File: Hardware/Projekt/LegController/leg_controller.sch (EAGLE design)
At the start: 53 parts, among them IC1 TS1117-3.3, IC3 ATXMEGA32A4U-AU, J1 22-27-2031-03, J2 22-27-2031-03, Q1 16MHz/18pF, T1 BC847SMD, T3 BC847SMD, T4 BC847SMD, U1 INA3221AIRGVT

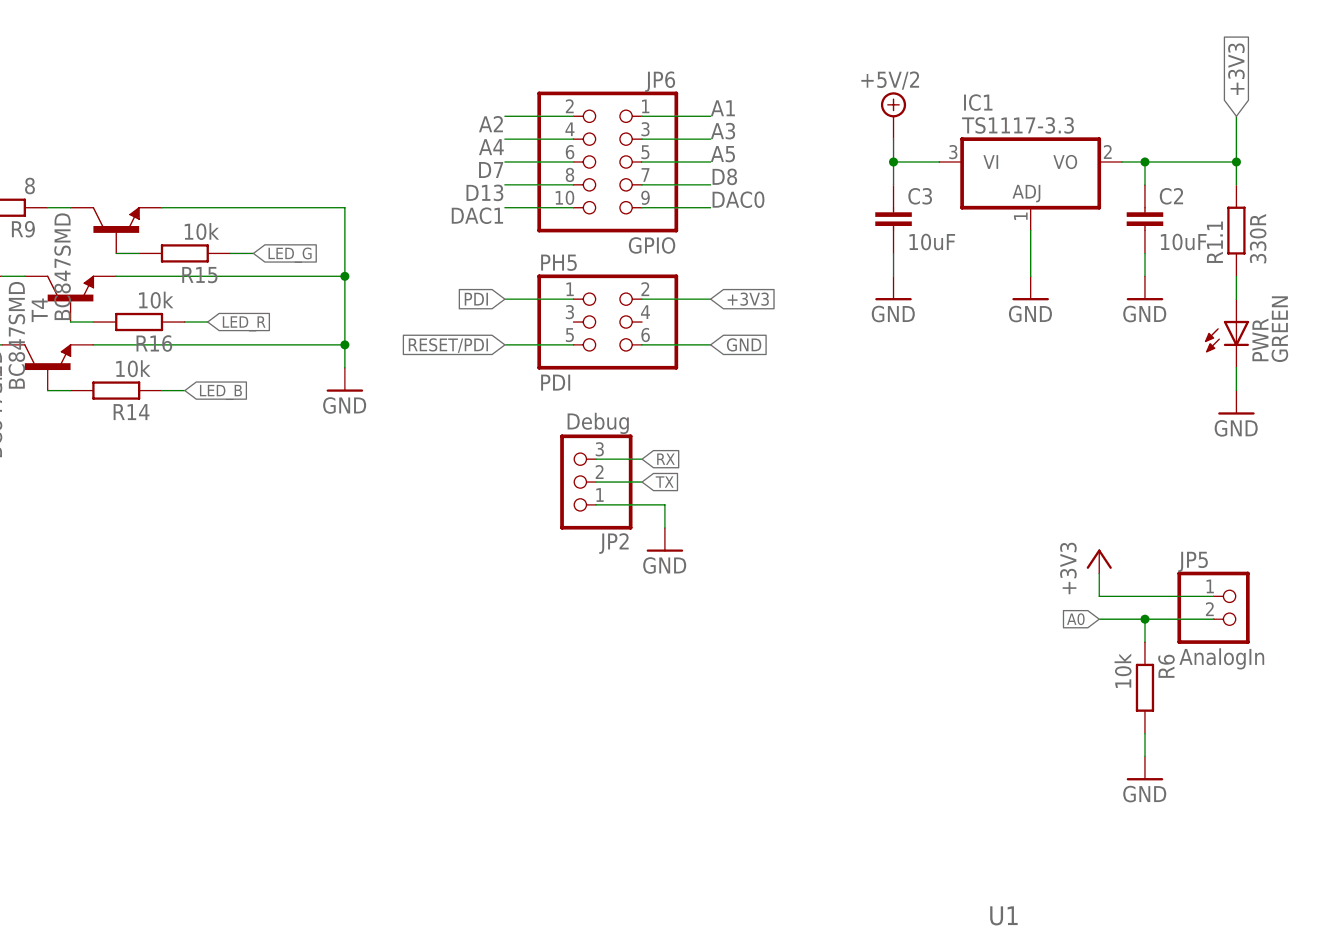
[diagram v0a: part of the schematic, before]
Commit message: Minor layout improvements
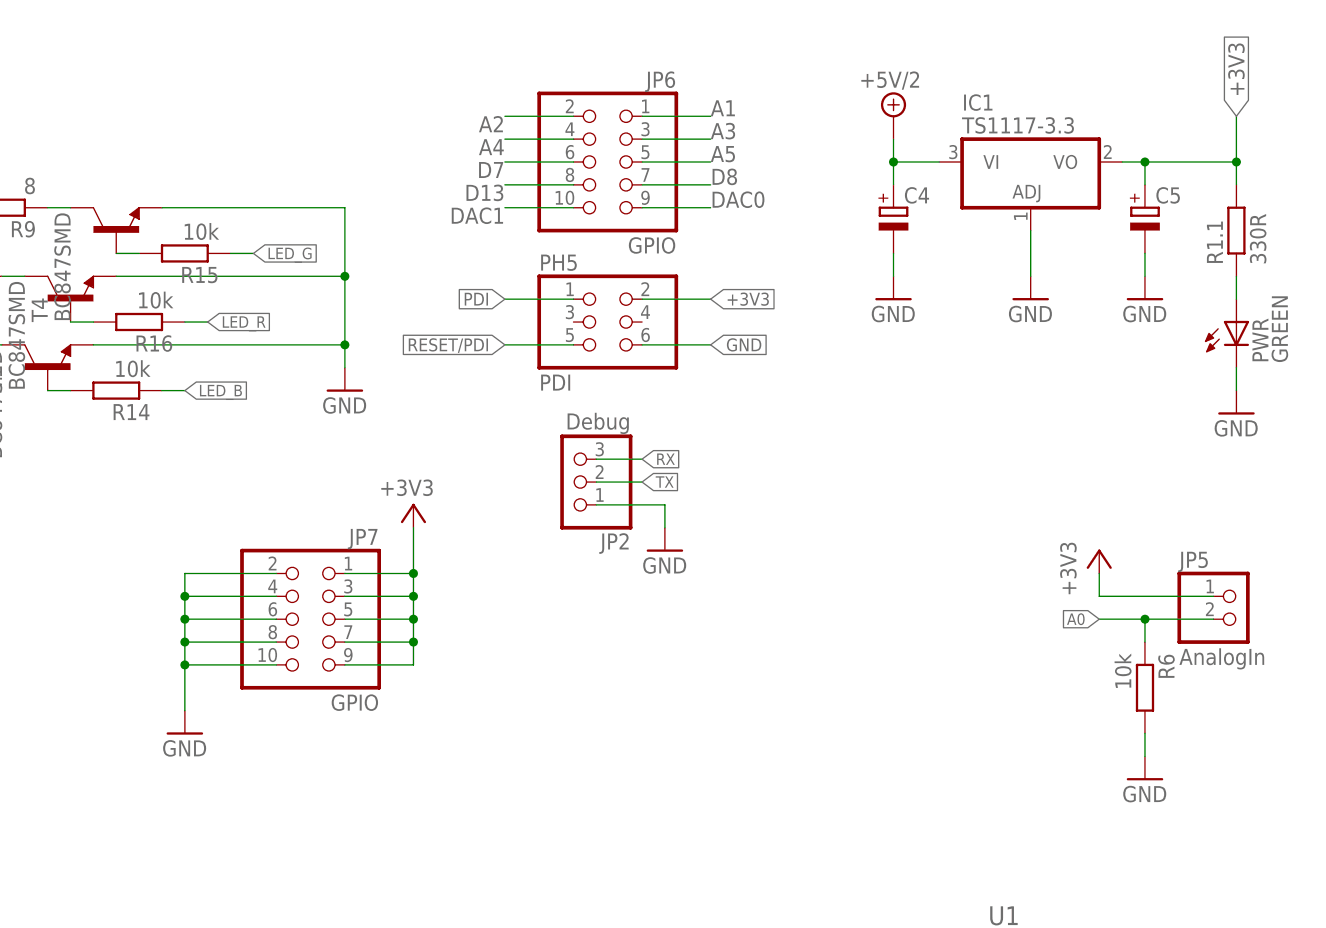
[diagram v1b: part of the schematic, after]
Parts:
- removed C2, C3: 10uF, rcl:C-EU025-024X044
- added C4, C5: (no value), rcl:CPOL-EUSMCA
- added JP7: GPIO, pinhead:PINHD-2X5
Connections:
- net +3V3: now also C5.+, JP7.1, JP7.3, JP7.5, JP7.7, JP7.9; no longer C2.1
- net +5V/2: now also C4.+; no longer C3.1
- net GND: now also C4.-, C5.-, JP7.10, JP7.2, JP7.4, JP7.6, JP7.8; no longer C2.2, C3.2
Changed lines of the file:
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@@
 <part name="SJ3" library="jumper" deviceset="SJ" device="" value="AD2"/>
 <part name="GND2" library="supply1" deviceset="GND" device=""/>
-<part name="C2" library="rcl" deviceset="C-EU" device="025-024X044" value="10uF"/>
-<part name="C3" library="rcl" deviceset="C-EU" device="025-024X044" value="10uF"/>
 <part name="GND14" library="supply1" deviceset="GND" device=""/>
+<part name="C4" library="rcl" deviceset="CPOL-EU" device="SMCA"/>
+<part name="C5" library="rcl" deviceset="CPOL-EU" device="SMCA"/>
+<part name="JP7" library="pinhead" deviceset="PINHD-2X5" device="" value="GPIO"/>
+<part name="+3V8" library="supply1" deviceset="+3V3" device=""/>
+<part name="GND15" library="supply1" deviceset="GND" device=""/>
 </parts>
 <sheets>
@@
 <instance part="SJ3" gate="1" x="17.78" y="12.7"/>
 <instance part="GND2" gate="1" x="27.94" y="7.62"/>
-<instance part="C2" gate="G$1" x="243.84" y="160.02"/>
-<instance part="C3" gate="G$1" x="215.9" y="160.02"/>
 <instance part="GND14" gate="1" x="215.9" y="149.86"/>
+<instance part="C4" gate="G$1" x="215.9" y="160.02"/>
+<instance part="C5" gate="G$1" x="243.84" y="160.02"/>
+<instance part="JP7" gate="A" x="152.4" y="114.3" rot="MR0"/>
+<instance part="+3V8" gate="G$1" x="162.56" y="127" smashed="yes">
+<attribute name="VALUE" x="158.75" y="128.016" size="1.778" layer="96"/>
+</instance>
+<instance part="GND15" gate="1" x="137.16" y="101.6"/>
 </instances>
 <busses>
@@
 </segment>
 <segment>
-<pinref part="C3" gate="G$1" pin="2"/>
 <pinref part="GND14" gate="1" pin="GND"/>
-<wire x1="215.9" y1="154.94" x2="215.9" y2="152.4" width="0.1524" layer="91"/>
-</segment>
-<segment>
-<pinref part="C2" gate="G$1" pin="2"/>
+<pinref part="C4" gate="G$1" pin="-"/>
+<wire x1="215.9" y1="152.4" x2="215.9" y2="154.94" width="0.1524" layer="91"/>
+</segment>
+<segment>
 <pinref part="GND25" gate="1" pin="GND"/>
-<wire x1="243.84" y1="154.94" x2="243.84" y2="152.4" width="0.1524" layer="91"/>
+<pinref part="C5" gate="G$1" pin="-"/>
+<wire x1="243.84" y1="152.4" x2="243.84" y2="154.94" width="0.1524" layer="91"/>
+</segment>
+<segment>
+<pinref part="JP7" gate="A" pin="10"/>
+<pinref part="GND15" gate="1" pin="GND"/>
+<wire x1="147.32" y1="109.22" x2="137.16" y2="109.22" width="0.1524" layer="91"/>
+<wire x1="137.16" y1="109.22" x2="137.16" y2="104.14" width="0.1524" layer="91"/>
+<pinref part="JP7" gate="A" pin="8"/>
+<wire x1="147.32" y1="111.76" x2="137.16" y2="111.76" width="0.1524" layer="91"/>
+<wire x1="137.16" y1="111.76" x2="137.16" y2="109.22" width="0.1524" layer="91"/>
+<junction x="137.16" y="109.22"/>
+<pinref part="JP7" gate="A" pin="6"/>
+<wire x1="147.32" y1="114.3" x2="137.16" y2="114.3" width="0.1524" layer="91"/>
+<wire x1="137.16" y1="114.3" x2="137.16" y2="111.76" width="0.1524" layer="91"/>
+<junction x="137.16" y="111.76"/>
+<pinref part="JP7" gate="A" pin="4"/>
+<wire x1="147.32" y1="116.84" x2="137.16" y2="116.84" width="0.1524" layer="91"/>
+<wire x1="137.16" y1="116.84" x2="137.16" y2="114.3" width="0.1524" layer="91"/>
+<junction x="137.16" y="114.3"/>
+<pinref part="JP7" gate="A" pin="2"/>
+<wire x1="147.32" y1="119.38" x2="137.16" y2="119.38" width="0.1524" layer="91"/>
+<wire x1="137.16" y1="119.38" x2="137.16" y2="116.84" width="0.1524" layer="91"/>
+<junction x="137.16" y="116.84"/>
 </segment>
 </net>
@@
 <wire x1="254" y1="162.56" x2="254" y2="165.1" width="0.1524" layer="91"/>
 <junction x="254" y="165.1"/>
-<pinref part="C2" gate="G$1" pin="1"/>
+<pinref part="C5" gate="G$1" pin="+"/>
 <wire x1="243.84" y1="162.56" x2="243.84" y2="165.1" width="0.1524" layer="91"/>
 <junction x="243.84" y="165.1"/>
@@
 <wire x1="251.46" y1="55.88" x2="256.54" y2="55.88" width="0.1524" layer="91"/>
 <wire x1="256.54" y1="55.88" x2="256.54" y2="58.42" width="0.1524" layer="91"/>
+</segment>
+<segment>
+<pinref part="+3V8" gate="G$1" pin="+3V3"/>
+<wire x1="162.56" y1="124.46" x2="162.56" y2="119.38" width="0.1524" layer="91"/>
+<pinref part="JP7" gate="A" pin="1"/>
+<wire x1="162.56" y1="119.38" x2="154.94" y2="119.38" width="0.1524" layer="91"/>
+<pinref part="JP7" gate="A" pin="3"/>
+<wire x1="154.94" y1="116.84" x2="162.56" y2="116.84" width="0.1524" layer="91"/>
+<wire x1="162.56" y1="116.84" x2="162.56" y2="119.38" width="0.1524" layer="91"/>
+<junction x="162.56" y="119.38"/>
+<pinref part="JP7" gate="A" pin="5"/>
+<wire x1="154.94" y1="114.3" x2="162.56" y2="114.3" width="0.1524" layer="91"/>
+<wire x1="162.56" y1="114.3" x2="162.56" y2="116.84" width="0.1524" layer="91"/>
+<junction x="162.56" y="116.84"/>
+<pinref part="JP7" gate="A" pin="7"/>
+<wire x1="154.94" y1="111.76" x2="162.56" y2="111.76" width="0.1524" layer="91"/>
+<wire x1="162.56" y1="111.76" x2="162.56" y2="114.3" width="0.1524" layer="91"/>
+<junction x="162.56" y="114.3"/>
+<pinref part="JP7" gate="A" pin="9"/>
+<wire x1="154.94" y1="109.22" x2="162.56" y2="109.22" width="0.1524" layer="91"/>
+<wire x1="162.56" y1="109.22" x2="162.56" y2="111.76" width="0.1524" layer="91"/>
+<junction x="162.56" y="111.76"/>
 </segment>
 </net>
@@
 <pinref part="SUPPLY1" gate="G$1" pin="+5V/2"/>
 <wire x1="215.9" y1="165.1" x2="215.9" y2="167.64" width="0.1524" layer="91"/>
-<pinref part="C3" gate="G$1" pin="1"/>
-<wire x1="215.9" y1="165.1" x2="215.9" y2="162.56" width="0.1524" layer="91"/>
+<pinref part="C4" gate="G$1" pin="+"/>
+<wire x1="215.9" y1="162.56" x2="215.9" y2="165.1" width="0.1524" layer="91"/>
 <junction x="215.9" y="165.1"/>
 </segment>
